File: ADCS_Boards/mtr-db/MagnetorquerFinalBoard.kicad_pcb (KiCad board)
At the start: 4 copper layers, 90.2 x 95.9 mm, 48 parts, among them J1 PC104_Connector, U1 X/Y_Coils, U2 Z_Coil

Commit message: adcs: mtr-db: updated design from Liam
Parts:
- QXF1, QXF2, QXR1, QXR2, QYF1, QYF2, QYR1, QYR2, QZF1, QZF2, QZR1, QZR2: value IRF540N -> IRLR120N
- moved QZR1 23.0 mm to (164.0, 86.0)
- moved QZF2 16.6 mm to (163.8, 102.0)
- moved QZF1 14.2 mm to (141.5, 86.0)
- moved QZR2 12.7 mm to (143.5, 102.0)
- moved C12 3.64 mm to (147.2, 95.2)
- moved UDZ1 3.64 mm to (147.2, 90.5)
- moved U2 1.47 mm to (189.3, 63.0)
- moved QYF1 1.43 mm to (166.7, 92.9)
- moved QYF2 1.43 mm to (166.7, 73.9)
- moved QYR1 1.43 mm to (166.7, 83.4)
- moved QYR2 1.43 mm to (166.7, 102.4)
- moved U1 1.40 mm to (196.6, 63.6)
- moved H7 1.14 mm to (173.8, 110.8)
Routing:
- net Z_COIL_A: track 27.6 -> 63.6 mm
- net Z_FWD: track 41.8 -> 60.1 mm, vias 2 -> 1
- net Z_REV: track 34.1 -> 50.5 mm, vias 2 -> 1
- net Z_COIL_B: track 31.5 -> 46.2 mm
- net Z_VCOIL: track 52.3 -> 63.6 mm, vias 1 -> 2
- net Enable: track 185.3 -> 191.9 mm, vias 4 -> 3
- net X_COIL_A: track 24.4 -> 28.8 mm
- net 5V: track 37.4 -> 41.4 mm
- net Y_COIL_B: track 18.4 -> 16.0 mm
- net Y_COIL_A: track 17.4 -> 19.7 mm
- net X_S: track 53.5 -> 51.9 mm
- net Z_S: track 49.7 -> 48.2 mm
- net Y_VCOIL: track 63.6 -> 62.3 mm
- net Y_REV: track 39.7 -> 38.6 mm
- net GND: track 88.8 -> 89.7 mm
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
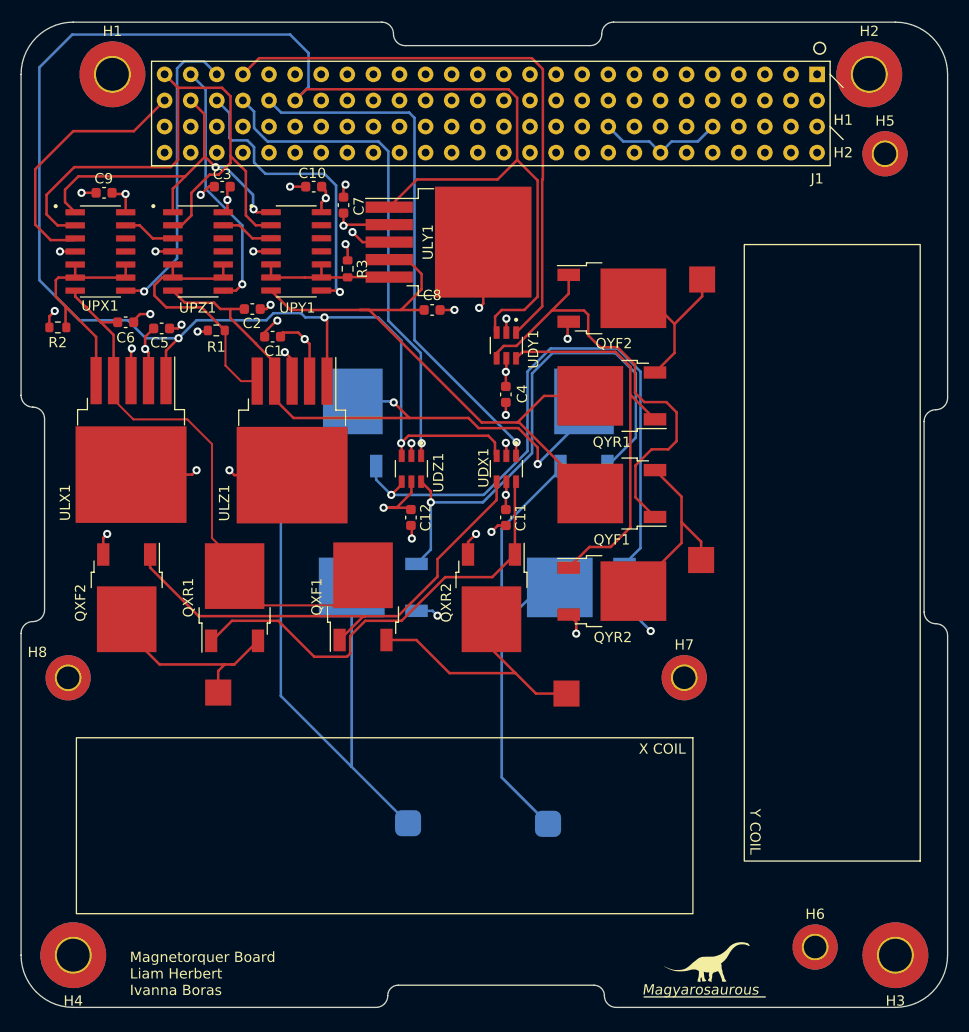
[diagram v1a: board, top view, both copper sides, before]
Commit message: adcs: mtr-db: minor changes to silkscreens
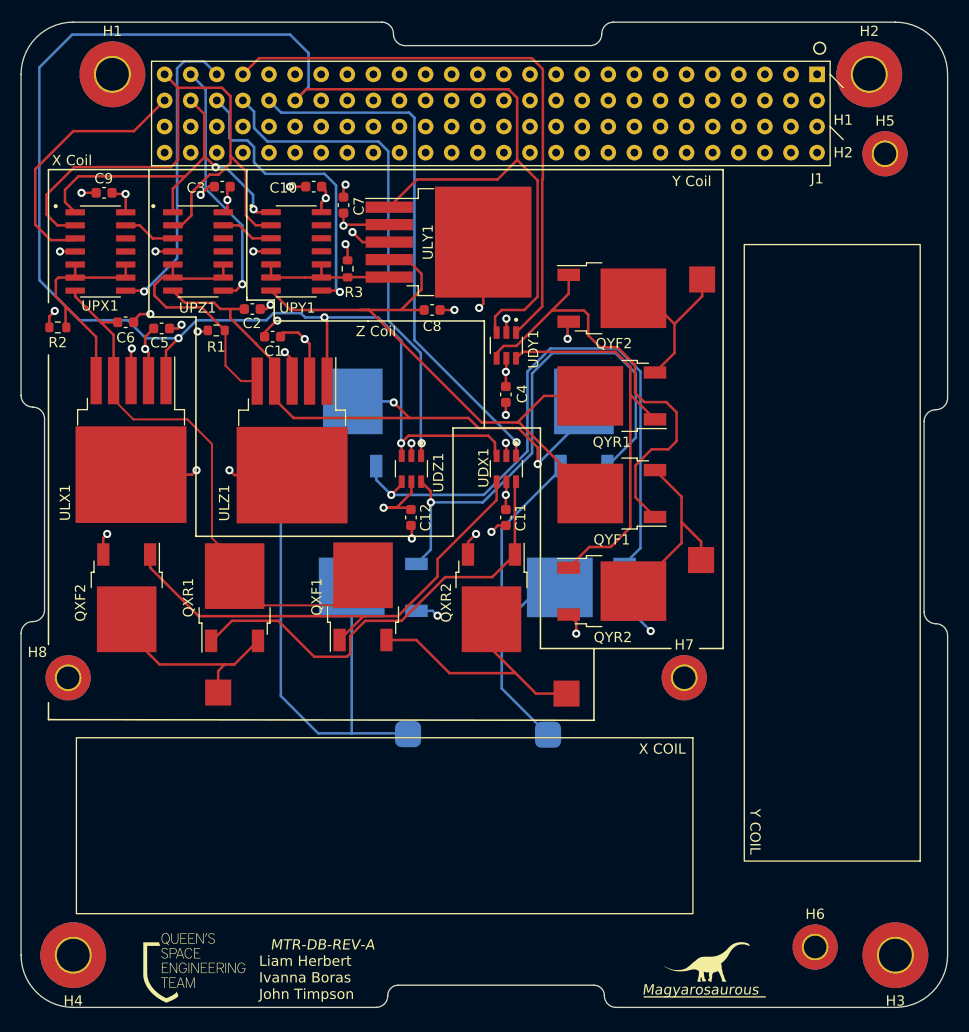
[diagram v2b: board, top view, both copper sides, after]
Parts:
- added G***: LOGO, LOGO, F.Cu at (126.1, 138.9)
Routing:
- net GND: track 89.7 -> 77.5 mm
- net Z_COIL_B: track 46.2 -> 37.6 mm
- net Z_COIL_A: track 63.6 -> 56.9 mm
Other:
- board text added: "Liam Herbert Ivanna Boras John Timpson"
- board text added: "MTR-DB-REV-A"
- board text added: "X Coil"
- board text added: "Y Coil"
- board text added: "Z Coil"
- board text removed: "Magnetorquer Board Liam Herbert Ivanna Boras"

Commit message: adcs: mtr-db: clean up schematic, include status LEDs in schematic
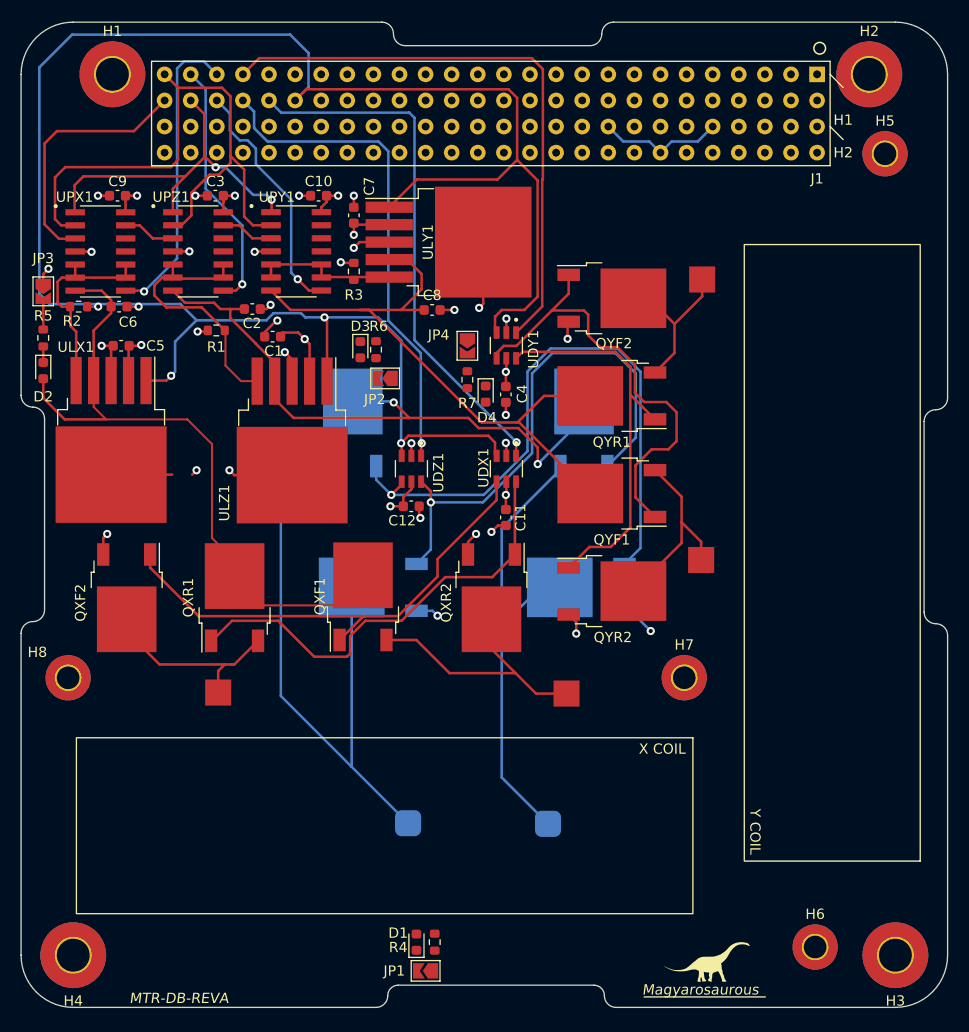
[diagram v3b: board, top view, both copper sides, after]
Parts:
- removed the G*** at (126.1, 138.9)
- added D1: ORANGE, LED_SMD:LED_0603_1608Metric, F.Cu at (147.7, 136.5)
- added D2: ORANGE, LED_SMD:LED_0603_1608Metric, F.Cu at (111.4, 80.9)
- added D3: ORANGE, LED_SMD:LED_0603_1608Metric, F.Cu at (142.2, 78.9)
- added D4: ORANGE, LED_SMD:LED_0603_1608Metric, F.Cu at (154.4, 83.2)
- added JP1: SolderJumper_2_Open, Jumper:SolderJumper-2_P1.3mm_Open_TrianglePad1.0x1.5mm, F.Cu at (148.6, 139.3)
- added JP2: SolderJumper_2_Open, Jumper:SolderJumper-2_P1.3mm_Open_TrianglePad1.0x1.5mm, F.Cu at (144.7, 81.7)
- added JP3: SolderJumper_2_Open, Jumper:SolderJumper-2_P1.3mm_Open_TrianglePad1.0x1.5mm, F.Cu at (111.4, 73.2)
- added JP4: SolderJumper_2_Open, Jumper:SolderJumper-2_P1.3mm_Open_TrianglePad1.0x1.5mm, F.Cu at (152.7, 78.5)
- added R4: 2k2, Resistor_SMD:R_0603_1608Metric, F.Cu at (149.5, 136.5)
- added R5: 2k2, Resistor_SMD:R_0603_1608Metric, F.Cu at (111.4, 77.7)
- added R6: 2k2, Resistor_SMD:R_0603_1608Metric, F.Cu at (143.8, 78.9)
- added R7: 2k2, Resistor_SMD:R_0603_1608Metric, F.Cu at (152.7, 81.8)
- moved C5 4.28 mm to (119.0, 78.5), turned to 180 degrees
- moved R2 2.86 mm to (114.8, 74.7), turned to 180 degrees
- moved ULX1 1.94 mm to (118.0, 87.7)
- moved C6 1.65 mm to (118.8, 74.7)
- moved C7 1.41 mm to (141.6, 65.8)
- moved C9 1.33 mm to (118.6, 63.9)
- moved C3 1.11 mm to (128.1, 63.9)
- moved C12 1.09 mm to (147.2, 94.1), turned to 0 degrees
- moved C10 1.00 mm to (138.2, 63.9)
- moved R3 0.65 mm to (141.6, 71.2)
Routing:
- net X_VCOIL: track 56.1 -> 67.7 mm
- net Z_COIL_B: track 37.6 -> 46.2 mm
- net GND: track 77.5 -> 84.3 mm, vias 33 -> 30
- net Z_COIL_A: track 56.9 -> 63.6 mm
- net Enable: track 191.9 -> 197.9 mm, vias 3 -> 5
- net Y_VCON: track 30.2 -> 24.4 mm
- net 5V: track 41.4 -> 36.9 mm
- net Net-(R5-Pad2): track 0.00 -> 2.98 mm
- net X_VADJ: track 25.1 -> 22.4 mm
- net Net-(D2-Pad1): track 0.00 -> 1.56 mm
- net SS: track 37.1 -> 36.1 mm
- net SCK: track 59.2 -> 60.2 mm, vias 0 -> 1
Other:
- board text added: "Liam Herbert Ivanna Boras"
- board text added: "MTR-DB-REVA"
- board text removed: "Liam Herbert Ivanna Boras John Timpson"
- board text removed: "MTR-DB-REV-A"
- board text removed: "X Coil"
- board text removed: "Y Coil"
- board text removed: "Z Coil"

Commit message: adcs: mtr-db: redo layout for smaller overall footprint, include status LEDs
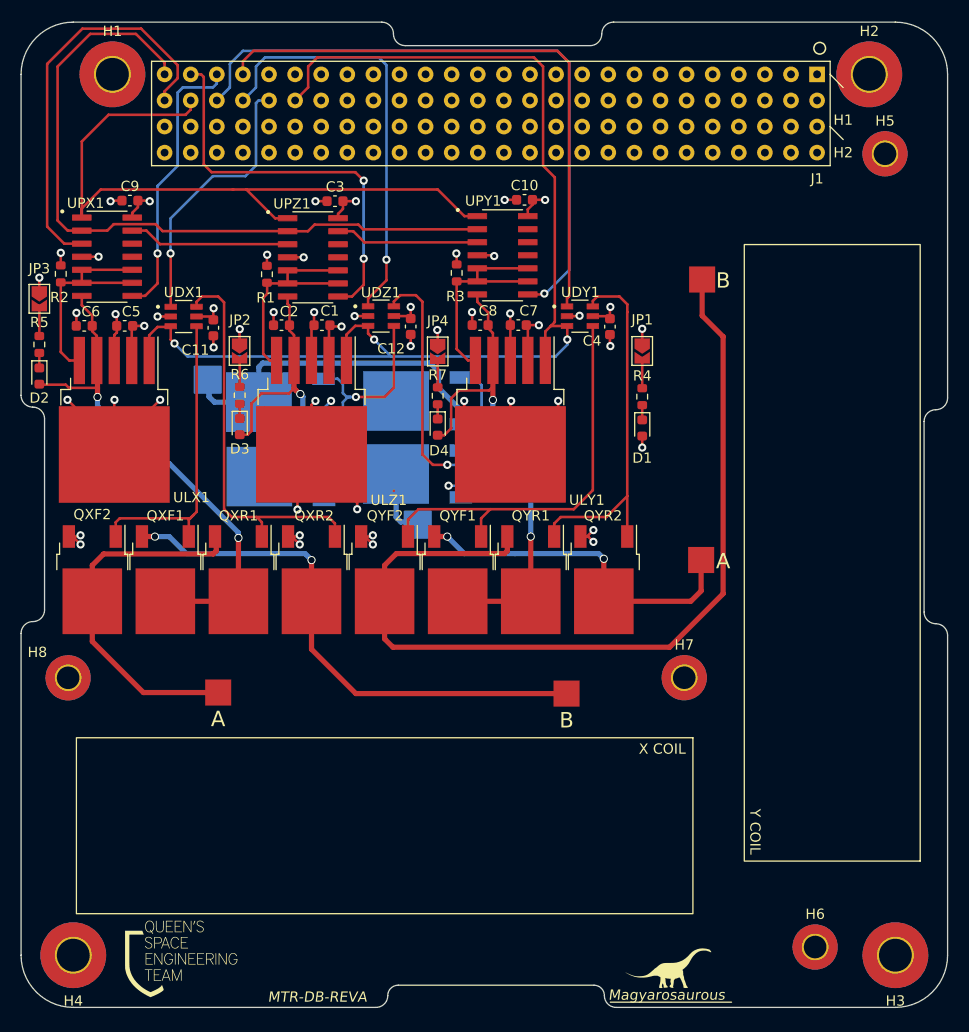
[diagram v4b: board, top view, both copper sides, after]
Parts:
- removed U2: Z_Coil, MCP42010-E_SL:ZCoil
- added G***: LOGO, LOGO, F.Cu at (124.8, 138.0)
- moved JP1 63.9 mm to (169.7, 79.0), turned to -90 degrees
- moved R4 56.8 mm to (169.7, 83.4), turned to 90 degrees
- moved D1 54.6 mm to (169.7, 86.5), turned to -90 degrees
- moved QYF2 35.2 mm to (144.6, 101.2), turned to -90 degrees
- moved UDX1 34.7 mm to (125.0, 75.6), turned to 0 degrees
- moved QZF2 34.4 mm to (134.5, 84.0)
- moved C11 33.9 mm to (127.9, 76.7)
- moved UPY1 20.1 mm to (156.1, 69.7)
- moved C10 20.0 mm to (158.2, 64.3)
- moved QYR1 19.5 mm to (158.8, 101.2), turned to -90 degrees
- moved QXF1 19.3 mm to (123.3, 101.2), turned to -90 degrees
- moved C7 19.2 mm to (157.6, 76.5), turned to 180 degrees
- moved ULY1 18.3 mm to (156.8, 85.7), turned to -90 degrees
- moved QXR2 17.6 mm to (137.5, 101.2)
- moved C12 17.5 mm to (147.1, 76.6), turned to -90 degrees
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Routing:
- net Enable: track 197.9 -> 115.2 mm, vias 5 -> 3
- net Y_COIL_B: track 16.0 -> 87.9 mm
- net GND: track 84.3 -> 154.6 mm, vias 30 -> 44
- net Z_COIL_A: track 63.6 -> 13.6 mm
- net Y_VCON: track 24.4 -> 63.3 mm
- net Z_FWD: track 60.1 -> 22.0 mm
- net SS: track 36.1 -> 66.6 mm, vias 2 -> 0
- net X_S: track 51.9 -> 26.5 mm
- net X_COIL_A: track 28.8 -> 52.7 mm, vias 0 -> 2
- net Z_VCOIL: track 63.6 -> 45.6 mm, vias 2 -> 1
- net X_VCOIL: track 67.7 -> 49.8 mm, vias 0 -> 2
- net X_FWD: track 47.9 -> 30.0 mm
- net X_COIL_B: track 19.3 -> 35.8 mm
- net Z_REV: track 50.5 -> 34.6 mm
- net Y_COIL_A: track 19.7 -> 34.4 mm, vias 0 -> 2
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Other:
- board text added: "A"
- board text added: "B"

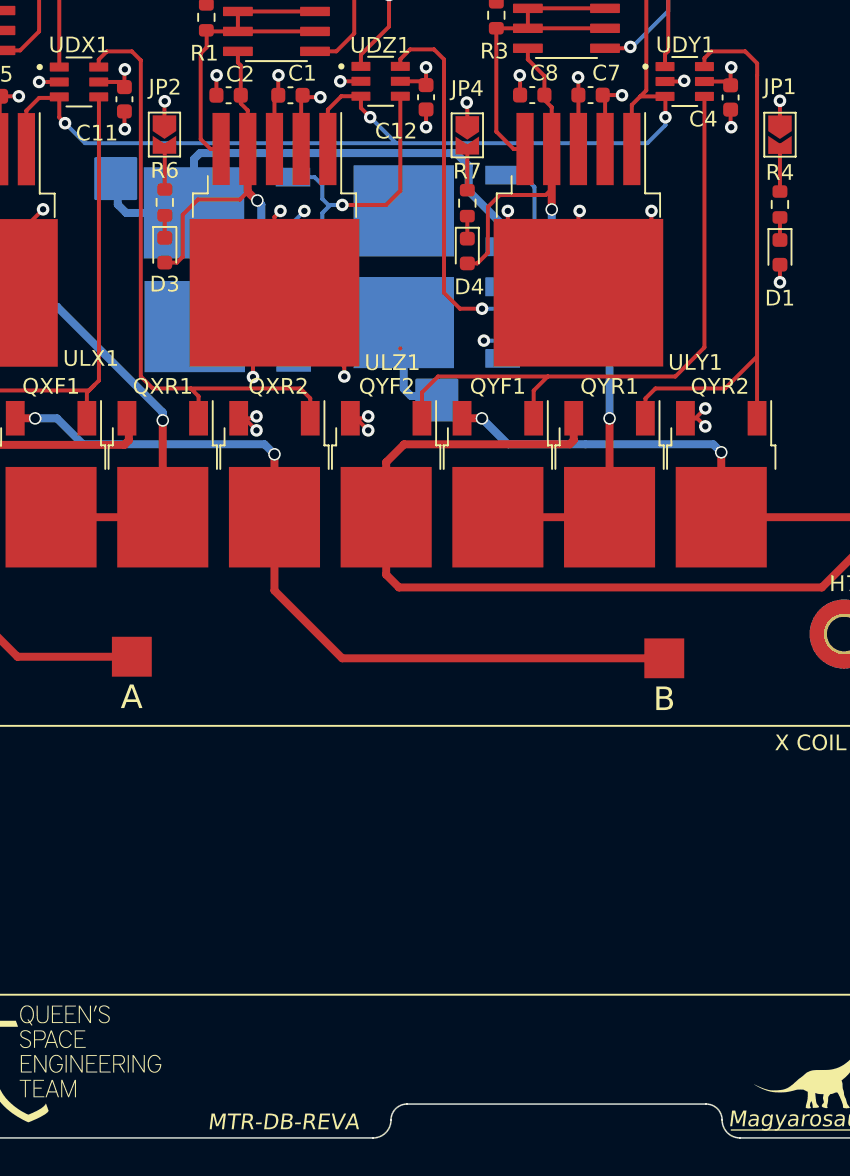
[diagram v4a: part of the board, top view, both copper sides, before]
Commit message: adcs: mtr-db: fixed back of PCB and updated silkscreen
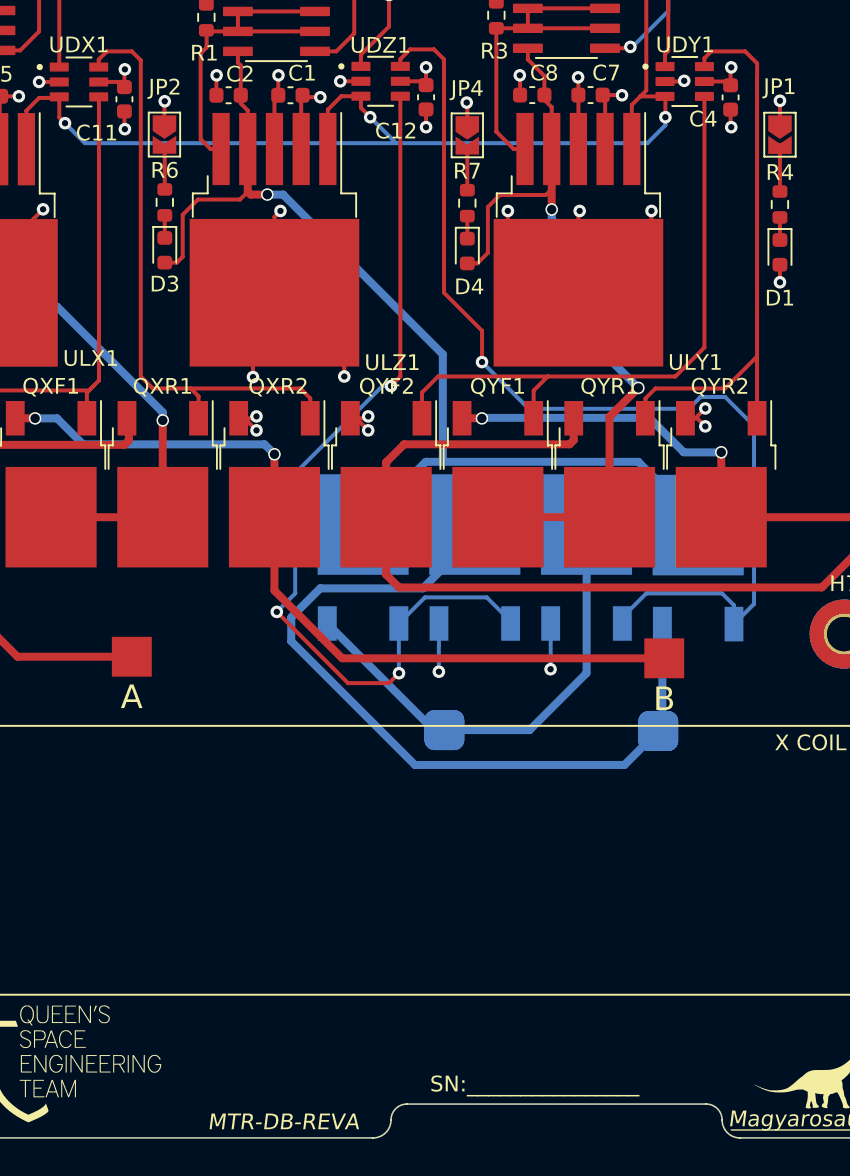
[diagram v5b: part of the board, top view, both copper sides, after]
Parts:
- added ?: , , F.Cu at (148.3, 116.9)
- added ?: , , F.Cu at (161.9, 117.0)
- added U2: Z_Coil, MCP42010-E_SL:ZCoil, B.Cu at (190.7, 63.6)
- moved QZR1 27.7 mm to (164.5, 106.0), turned to 90 degrees
- moved QZF2 27.0 mm to (150.2, 105.9), turned to 90 degrees
- moved QZR2 17.7 mm to (157.4, 105.9), turned to 90 degrees
- moved QZF1 17.0 mm to (143.1, 105.9), turned to 90 degrees
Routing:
- net Z_FWD: track 22.0 -> 58.1 mm, vias 1 -> 3
- net Z_REV: track 34.6 -> 66.4 mm
- net Z_VCOIL: track 45.6 -> 66.3 mm
- net Z_COIL_B: track 34.1 -> 50.8 mm
- net Z_COIL_A: track 13.6 -> 30.3 mm
- net Y_VCOIL: track 50.7 -> 52.2 mm
- net GND: track 154.6 -> 155.7 mm
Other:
- board text added: "Liam Herbert Ivanna Boras John Timpson"
- board text added: "SN:________________"
- board text removed: "Liam Herbert Ivanna Boras"
